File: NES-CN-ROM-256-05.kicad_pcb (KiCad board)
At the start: 2 copper layers, 100.3 x 54.9 mm, 14 parts, among them U2 74HC161, U3 ATtiny13A-PU, U4 CHR-ROM, U5 PRG-ROM

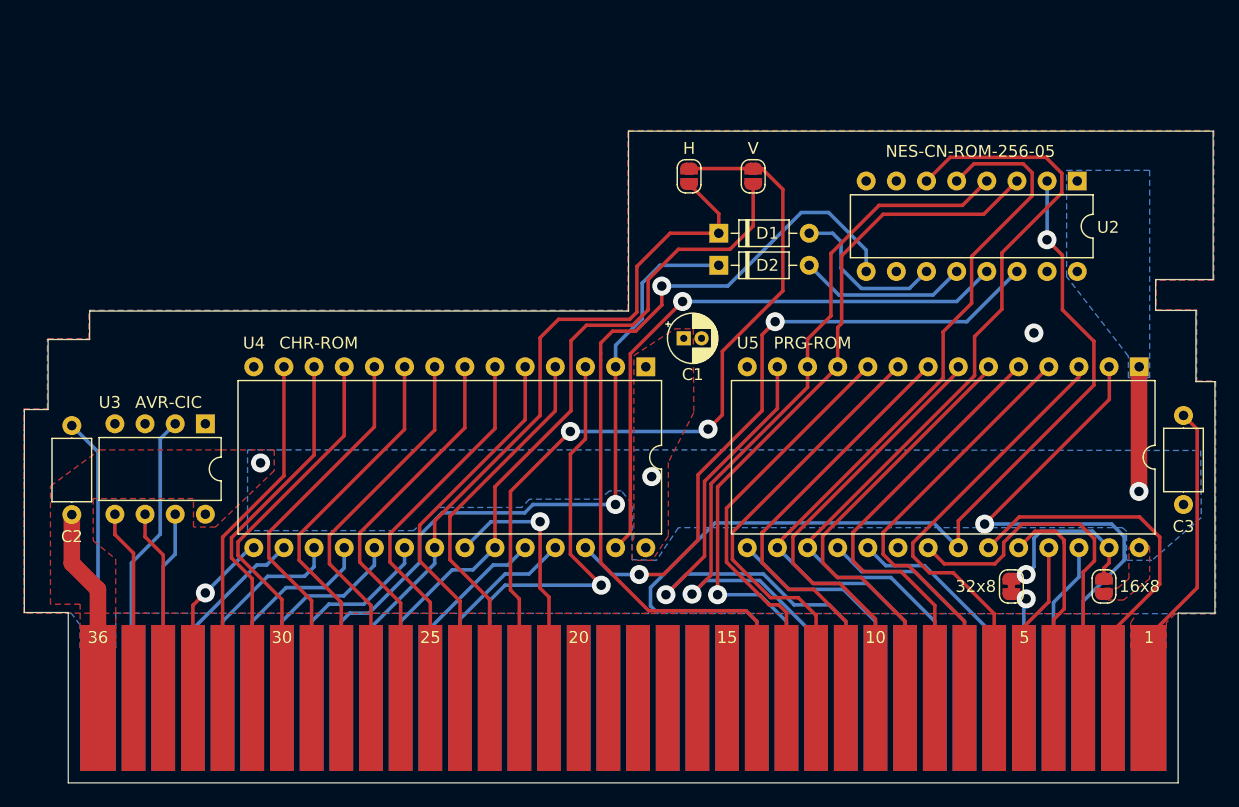
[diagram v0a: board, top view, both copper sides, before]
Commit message: [1] Change gerbers to protel file ext [2] Fix board dimensions [3] Add screenshot of jlcpcb order settings
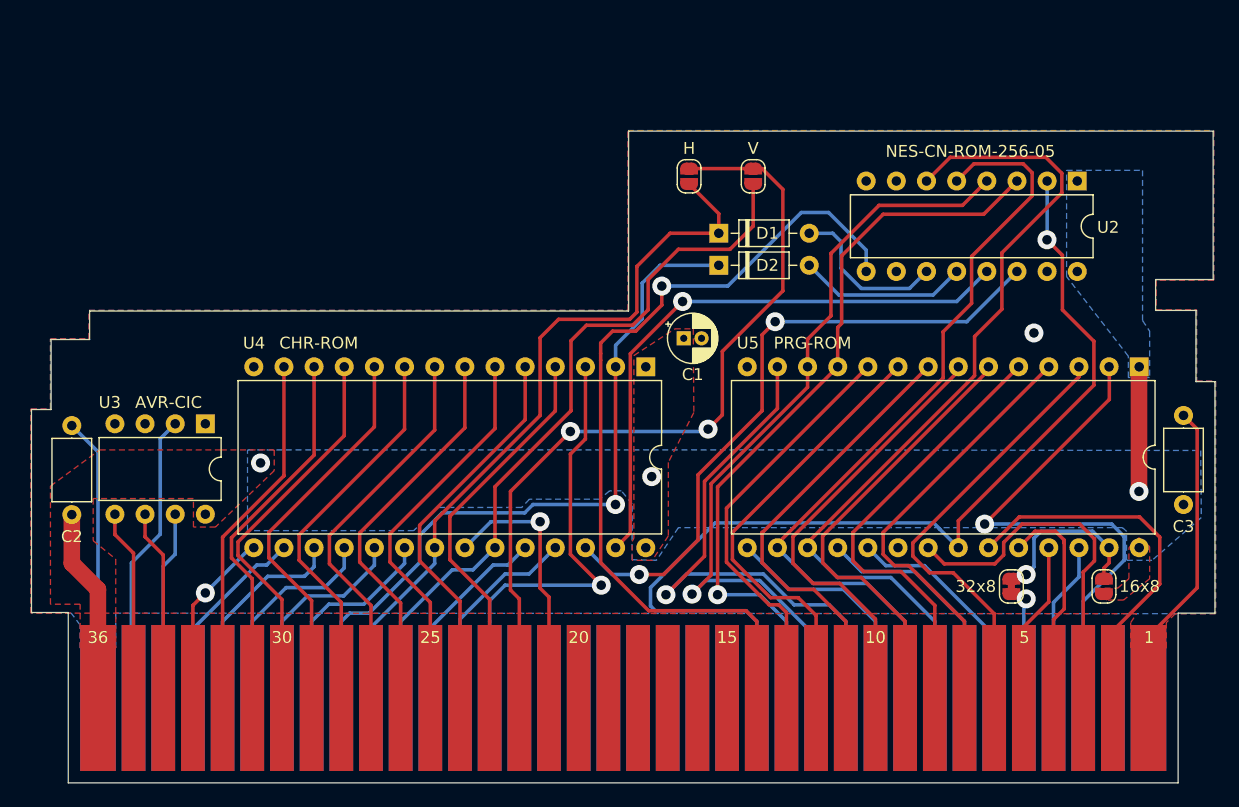
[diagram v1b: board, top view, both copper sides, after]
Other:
- board size 100.3 x 54.9 mm -> 99.7 x 54.9 mm
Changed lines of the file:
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@@
   (title_block
     (title "NES-CN-ROM-256-05 PCB")
-    (date 2022-04-25)
+    (date 2022-04-26)
     (rev v01)
     (comment 1 "License: https://creativecommons.org/licenses/by-sa/4.0/")
@@
     (visible_elements 7FFFFFFF)
     (pcbplotparams
-      (layerselection 0x010f0_ffffffff)
-      (usegerberextensions false)
-      (usegerberattributes true)
-      (usegerberadvancedattributes true)
+      (layerselection 0x010fc_ffffffff)
+      (usegerberextensions true)
+      (usegerberattributes false)
+      (usegerberadvancedattributes false)
       (creategerberjobfile false)
       (excludeedgelayer true)
@@
       (psa4output false)
       (plotreference true)
-      (plotvalue false)
+      (plotvalue true)
       (plotinvisibletext false)
       (padsonsilk false)
-      (subtractmaskfromsilk false)
+      (subtractmaskfromsilk true)
       (outputformat 1)
       (mirror false)
@@
       ))
   )
-  (dimension 3.7 (width 0.15) (layer Dwgs.User)
-    (gr_text "3.700 mm" (at 114.65 131.25) (layer Dwgs.User)
+  (dimension 3.1 (width 0.15) (layer Dwgs.User)
+    (gr_text "3.100 mm" (at 114.95 131.25) (layer Dwgs.User)
       (effects (font (size 1 1) (thickness 0.15)))
     )
     (feature1 (pts (xy 116.5 110.65) (xy 116.5 130.536421)))
-    (feature2 (pts (xy 112.8 110.65) (xy 112.8 130.536421)))
-    (crossbar (pts (xy 112.8 129.95) (xy 116.5 129.95)))
+    (feature2 (pts (xy 113.4 110.65) (xy 113.4 130.536421)))
+    (crossbar (pts (xy 113.4 129.95) (xy 116.5 129.95)))
     (arrow1a (pts (xy 116.5 129.95) (xy 115.373496 130.536421)))
     (arrow1b (pts (xy 116.5 129.95) (xy 115.373496 129.363579)))
-    (arrow2a (pts (xy 112.8 129.95) (xy 113.926504 130.536421)))
-    (arrow2b (pts (xy 112.8 129.95) (xy 113.926504 129.363579)))
+    (arrow2a (pts (xy 113.4 129.95) (xy 114.526504 130.536421)))
+    (arrow2b (pts (xy 113.4 129.95) (xy 114.526504 129.363579)))
   )
   (dimension 3.1 (width 0.15) (layer Dwgs.User)
@@
     (arrow2b (pts (xy 213.1 129.95) (xy 211.973496 130.536421)))
   )
-  (dimension 2 (width 0.15) (layer Dwgs.User)
-    (gr_text "2.000 mm" (at 113.8 82.7) (layer Dwgs.User)
-      (effects (font (size 1 1) (thickness 0.15)))
-    )
-    (feature1 (pts (xy 114.8 93.55) (xy 114.8 83.413579)))
-    (feature2 (pts (xy 112.8 93.55) (xy 112.8 83.413579)))
-    (crossbar (pts (xy 112.8 84) (xy 114.8 84)))
-    (arrow1a (pts (xy 114.8 84) (xy 113.673496 84.586421)))
-    (arrow1b (pts (xy 114.8 84) (xy 113.673496 83.413579)))
-    (arrow2a (pts (xy 112.8 84) (xy 113.926504 84.586421)))
-    (arrow2b (pts (xy 112.8 84) (xy 113.926504 83.413579)))
+  (dimension 1.65 (width 0.15) (layer Dwgs.User)
+    (gr_text "1.650 mm" (at 114.225 82.7) (layer Dwgs.User)
+      (effects (font (size 1 1) (thickness 0.15)))
+    )
+    (feature1 (pts (xy 115.05 93.55) (xy 115.05 83.413579)))
+    (feature2 (pts (xy 113.4 93.55) (xy 113.4 83.413579)))
+    (crossbar (pts (xy 113.4 84) (xy 115.05 84)))
+    (arrow1a (pts (xy 115.05 84) (xy 113.923496 84.586421)))
+    (arrow1b (pts (xy 115.05 84) (xy 113.923496 83.413579)))
+    (arrow2a (pts (xy 113.4 84) (xy 114.526504 84.586421)))
+    (arrow2b (pts (xy 113.4 84) (xy 114.526504 83.413579)))
   )
   (dimension 45.4 (width 0.15) (layer Dwgs.User)
@@
     (arrow2b (pts (xy 118.3 66.5) (xy 119.426504 65.913579)))
   )
-  (dimension 3.5 (width 0.15) (layer Dwgs.User)
-    (gr_text "3.500 mm" (at 116.55 78.7) (layer Dwgs.User)
+  (dimension 3.25 (width 0.15) (layer Dwgs.User)
+    (gr_text "3.250 mm" (at 116.675 78.7) (layer Dwgs.User)
       (effects (font (size 1 1) (thickness 0.15)))
     )
     (feature1 (pts (xy 118.3 87.65) (xy 118.3 79.413579)))
-    (feature2 (pts (xy 114.8 87.65) (xy 114.8 79.413579)))
-    (crossbar (pts (xy 114.8 80) (xy 118.3 80)))
+    (feature2 (pts (xy 115.05 87.65) (xy 115.05 79.413579)))
+    (crossbar (pts (xy 115.05 80) (xy 118.3 80)))
     (arrow1a (pts (xy 118.3 80) (xy 117.173496 80.586421)))
     (arrow1b (pts (xy 118.3 80) (xy 117.173496 79.413579)))
-    (arrow2a (pts (xy 114.8 80) (xy 115.926504 80.586421)))
-    (arrow2b (pts (xy 114.8 80) (xy 115.926504 79.413579)))
+    (arrow2a (pts (xy 115.05 80) (xy 116.176504 80.586421)))
+    (arrow2b (pts (xy 115.05 80) (xy 116.176504 79.413579)))
   )
   (dimension 5.9 (width 0.15) (layer Dwgs.User)
@@
   )
   (gr_line (start 116.5 110.65) (end 116.5 110.7) (layer Edge.Cuts) (width 0.05))
-  (gr_line (start 112.8 110.65) (end 116.5 110.65) (layer Edge.Cuts) (width 0.05))
-  (gr_line (start 112.8 93.55) (end 112.8 110.65) (layer Edge.Cuts) (width 0.05))
-  (gr_line (start 114.8 93.55) (end 112.8 93.55) (layer Edge.Cuts) (width 0.05))
-  (gr_line (start 114.8 87.65) (end 114.8 93.55) (layer Edge.Cuts) (width 0.05))
-  (gr_line (start 118.3 87.65) (end 114.8 87.65) (layer Edge.Cuts) (width 0.05))
+  (gr_line (start 113.4 110.65) (end 116.5 110.65) (layer Edge.Cuts) (width 0.05))
+  (gr_line (start 113.4 93.55) (end 113.4 110.65) (layer Edge.Cuts) (width 0.05))
+  (gr_line (start 115.05 93.55) (end 113.4 93.55) (layer Edge.Cuts) (width 0.05))
+  (gr_line (start 115.05 87.65) (end 115.05 93.55) (layer Edge.Cuts) (width 0.05))
+  (gr_line (start 118.3 87.65) (end 115.05 87.65) (layer Edge.Cuts) (width 0.05))
   (gr_line (start 118.3 85.25) (end 118.3 87.65) (layer Edge.Cuts) (width 0.05))
   (gr_line (start 163.7 85.25) (end 118.3 85.25) (layer Edge.Cuts) (width 0.05))
@@
     (polygon
       (pts
-        (xy 207.6 90.85) (xy 205.8 90.85) (xy 205.8 89.05) (xy 200.6 82.35) (xy 200.6 73.4)
-        (xy 207.6 73.4)
+        (xy 207 86.05) (xy 207.6 86.95) (xy 207.6 90.85) (xy 205.8 90.85) (xy 205.8 89.05)
+        (xy 200.6 82.35) (xy 200.6 73.4) (xy 207 73.4)
       )
     )
@@
         (xy 213 82.65) (xy 208.15 82.65) (xy 208.15 85.15) (xy 211.55 85.15) (xy 211.55 91.15)
         (xy 213.15 91.15) (xy 213.15 110.75) (xy 209.75 110.75) (xy 209 111.5) (xy 209 113.65)
-        (xy 206 113.65) (xy 206 111.5) (xy 206.5 110.75) (xy 112.75 110.7) (xy 112.75 93.5)
-        (xy 114.75 93.5) (xy 114.75 87.6) (xy 118.25 87.6) (xy 118.25 85.2) (xy 163.65 85.2)
+        (xy 206 113.65) (xy 206 111.5) (xy 206.5 110.75) (xy 113.35 110.7) (xy 113.35 93.5)
+        (xy 115 93.5) (xy 115 87.6) (xy 118.25 87.6) (xy 118.25 85.2) (xy 163.65 85.2)
         (xy 163.65 70.05) (xy 213 70.05)
       )
@@
         (xy 213 82.65) (xy 208.15 82.65) (xy 208.15 85.15) (xy 211.55 85.15) (xy 211.55 91.15)
         (xy 213.15 91.15) (xy 213.15 110.75) (xy 120.5 110.70401) (xy 120.5 113.65) (xy 117.5 113.65)
-        (xy 117.5 111.7) (xy 116.75 110.7) (xy 112.75 110.7) (xy 112.75 93.5) (xy 114.75 93.5)
-        (xy 114.75 87.6) (xy 118.25 87.6) (xy 118.25 85.2) (xy 163.65 85.2) (xy 163.65 70.05)
+        (xy 117.5 111.7) (xy 116.75 110.7) (xy 113.35 110.7) (xy 113.35 93.5) (xy 115 93.5)
+        (xy 115 87.6) (xy 118.25 87.6) (xy 118.25 85.2) (xy 163.65 85.2) (xy 163.65 70.05)
         (xy 213 70.05)
       )

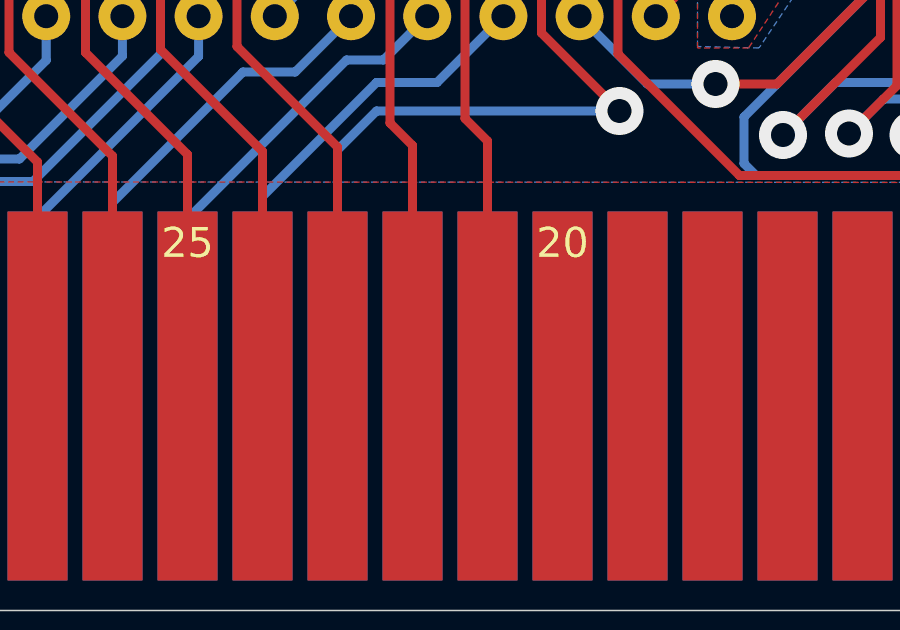
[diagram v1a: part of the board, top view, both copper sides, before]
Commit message: [1] Connect cartridge pins 57-58 for NES internal VRAM enable line. [2] Regenerate gerbers.
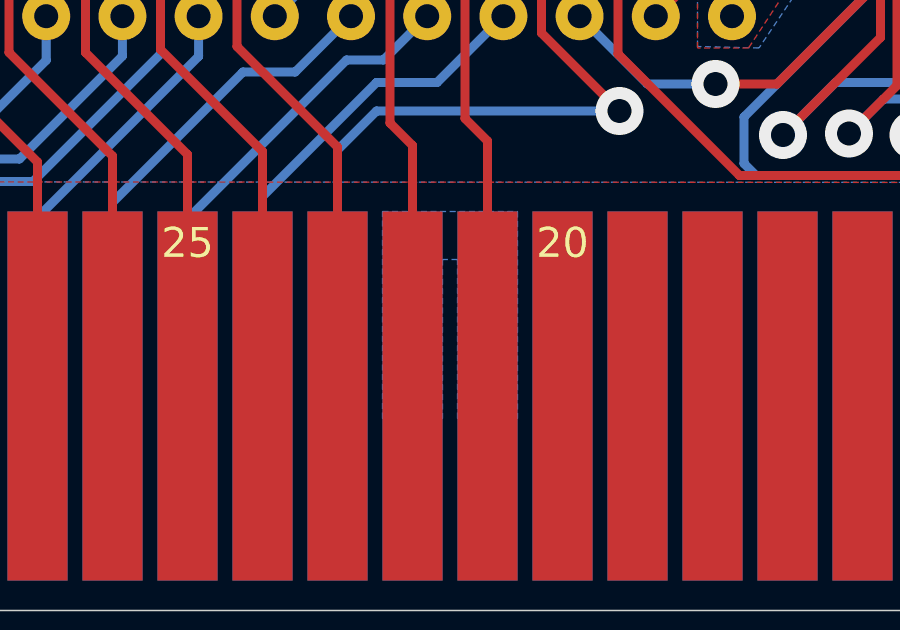
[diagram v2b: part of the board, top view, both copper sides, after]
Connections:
- EDGE1 pad 57: (no net) -> Net-(EDGE1-Pad57)
- EDGE1 pad 58: (no net) -> Net-(EDGE1-Pad57)
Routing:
- added copper zone on B.Cu, net Net-(EDGE1-Pad57)
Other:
- net class VRAM_Enable added: clearance 0.2, trace_width 2, via_dia 1.6, via_drill 0.8
- board text added: "v01.1"
- board text removed: "v01"

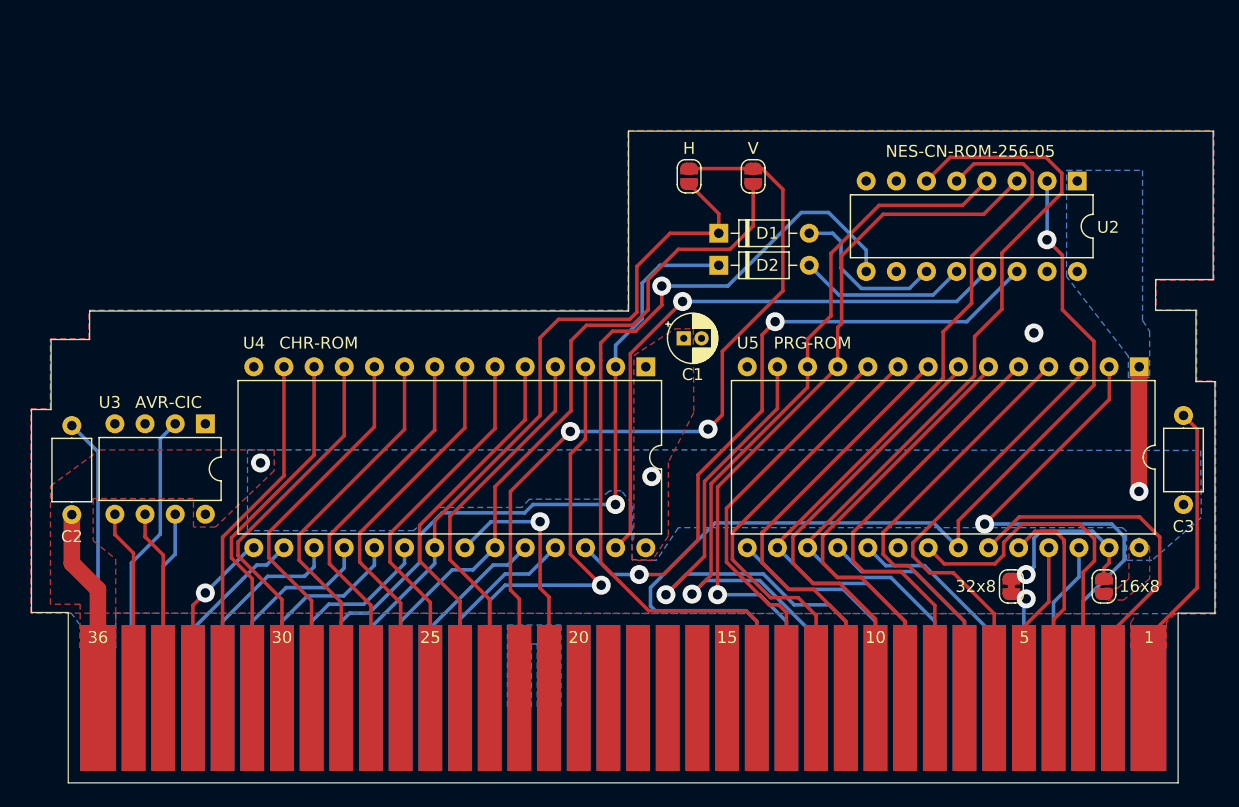
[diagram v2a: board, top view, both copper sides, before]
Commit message: New board layout to support 32 dip flash chips
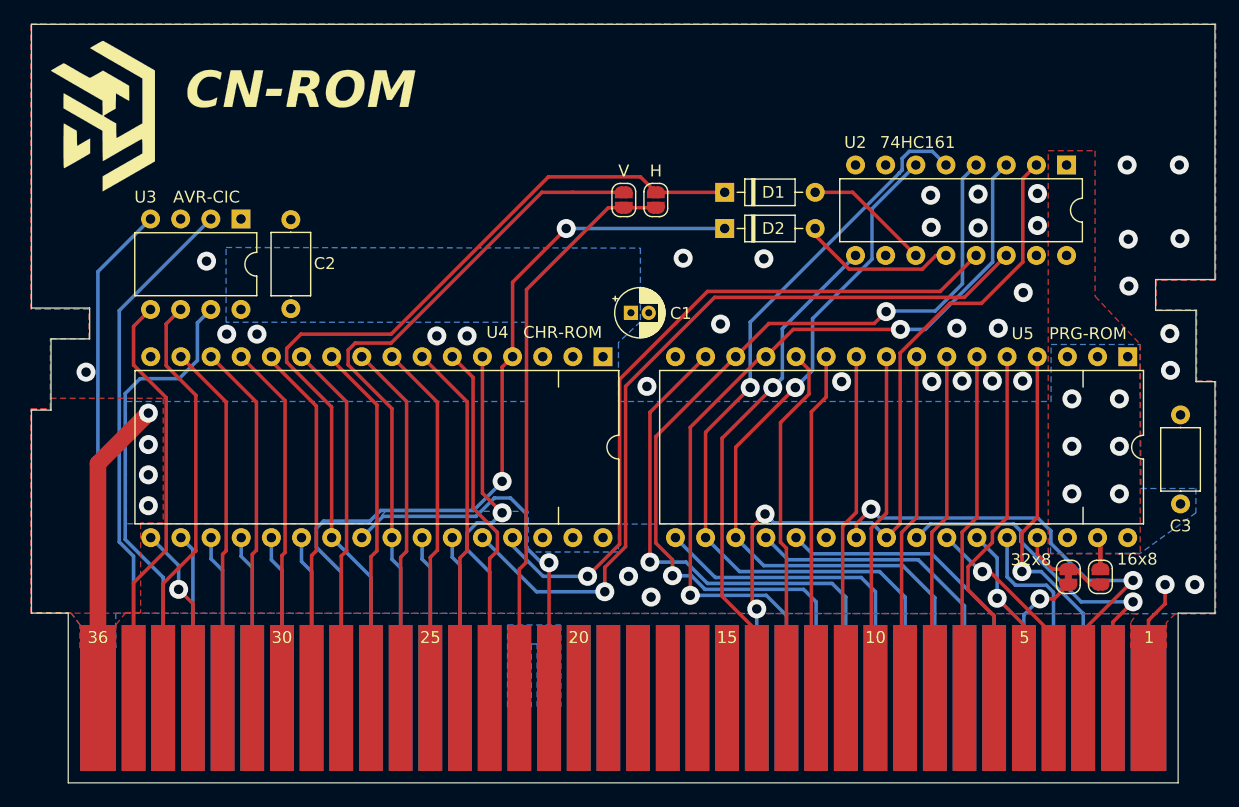
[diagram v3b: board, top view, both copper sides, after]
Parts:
- added G1: LOGO, logo:flash_logo, F.Cu at (119.4, 69.5)
- added G2: LOGO, logo:flash_negative_logo, F.Cu at (119.4, 69.5)
- added G3: LOGO, logo:cnrom_text, F.Cu at (136.0, 66.5)
- U4, U5: footprint Package_DIP:DIP-28_W15.24mm -> Package_DIP:DIP-32_W15.24mm
- moved C2 25.3 mm to (135.2, 85.0)
- moved U3 17.5 mm to (131.1, 77.5)
- moved JP4 11.1 mm to (163.3, 75.9), turned to 270 degrees
- moved C1 4.94 mm to (163.9, 85.4)
- moved JP1 4.87 mm to (200.8, 107.7)
- moved U4 3.70 mm to (161.6, 89.1)
- moved D1 3.49 mm to (171.8, 75.2)
- moved JP3 3.44 mm to (166.0, 75.9), turned to 270 degrees
- moved D2 3.14 mm to (171.8, 78.3)
- moved U2 1.62 mm to (200.6, 73.0)
- moved U5 1.29 mm to (205.8, 89.1)
- moved JP2 0.85 mm to (203.4, 107.7), turned to 270 degrees
- moved C3 0.25 mm to (210.2, 101.5)
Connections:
- U4 pad 10: PPU_A0 -> PPU_A2
- U4 pad 11: PPU_AD0 -> PPU_A1
- U4 pad 12: PPU_AD1 -> PPU_A0
- U4 pad 13: PPU_AD2 -> PPU_AD0
- U4 pad 14: GND -> PPU_AD1
- U4 pad 15: PPU_AD3 -> PPU_AD2
- U4 pad 16: PPU_AD4 -> GND
- U4 pad 17: PPU_AD5 -> PPU_AD3
- U4 pad 18: PPU_AD6 -> PPU_AD4
- U4 pad 19: PPU_AD7 -> PPU_AD5
- U4 pad 2: PPU_A12 -> +5V
- U4 pad 20: PPU_A13 -> PPU_AD6
- U4 pad 21: PPU_A10 -> PPU_AD7
- U4 pad 22: PPU_RD -> PPU_A13
- U4 pad 23: PPU_A11 -> PPU_A10
- U4 pad 24: PPU_A9 -> PPU_RD
- U4 pad 25: PPU_A8 -> PPU_A11
- U4 pad 26: /CHR_A13 -> PPU_A9
- U4 pad 27: /CHR_A14 -> PPU_A8
- U4 pad 28: +5V -> /CHR_A13
- U4 pad 3: PPU_A7 -> +5V
- U4 pad 4: PPU_A6 -> PPU_A12
- U4 pad 5: PPU_A5 -> PPU_A7
- U4 pad 6: PPU_A4 -> PPU_A6
- U4 pad 7: PPU_A3 -> PPU_A5
- U4 pad 8: PPU_A2 -> PPU_A4
- U4 pad 9: PPU_A1 -> PPU_A3
- U5 pad 10: CPU_A0 -> CPU_A2
- U5 pad 11: CPU_D0 -> CPU_A1
- U5 pad 12: CPU_D1 -> CPU_A0
- U5 pad 13: CPU_D2 -> CPU_D0
- U5 pad 14: GND -> CPU_D1
- U5 pad 15: CPU_D3 -> CPU_D2
- U5 pad 16: CPU_D4 -> GND
- U5 pad 17: CPU_D5 -> CPU_D3
- U5 pad 18: CPU_D6 -> CPU_D4
- U5 pad 19: CPU_D7 -> CPU_D5
- U5 pad 2: CPU_A12 -> +5V
- U5 pad 20: GND -> CPU_D6
- U5 pad 21: CPU_A10 -> CPU_D7
- U5 pad 22: ROMSEL -> GND
- U5 pad 23: CPU_A11 -> CPU_A10
- U5 pad 24: CPU_A9 -> ROMSEL
- U5 pad 25: CPU_A8 -> CPU_A11
- U5 pad 26: CPU_A13 -> CPU_A9
- U5 pad 27: /PRG_A14 -> CPU_A8
- U5 pad 28: +5V -> CPU_A13
- U5 pad 3: CPU_A7 -> +5V
- U5 pad 4: CPU_A6 -> CPU_A12
- U5 pad 5: CPU_A5 -> CPU_A7
- U5 pad 6: CPU_A4 -> CPU_A6
- U5 pad 7: CPU_A3 -> CPU_A5
- U5 pad 8: CPU_A2 -> CPU_A4
- U5 pad 9: CPU_A1 -> CPU_A3
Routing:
- net CPU_RW: track 71.1 -> 43.1 mm
- net CIC_RST: track 15.9 -> 39.0 mm
- net CIRAM_A10: track 68.0 -> 48.4 mm, vias 2 -> 0
- net CIC_IN: track 16.1 -> 35.6 mm
- net CIC_CLK: track 24.7 -> 44.0 mm
- net CIC_OUT: track 16.1 -> 35.4 mm
- net ROMSEL: track 83.8 -> 65.3 mm, vias 1 -> 2
- net PPU_A10: track 62.4 -> 75.8 mm
- net /CHR_A13: track 54.8 -> 66.9 mm, vias 2 -> 1
- net /CHR_A14: track 49.8 -> 60.1 mm
- net PPU_RD: track 22.4 -> 32.5 mm
- net CPU_A5: track 38.4 -> 29.4 mm
- net CPU_A10: track 30.9 -> 39.7 mm, vias 0 -> 2
- net CPU_A1: track 38.0 -> 29.4 mm
- net CPU_A2: track 37.9 -> 29.3 mm
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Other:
- board size 99.7 x 54.9 mm -> 99.7 x 63.9 mm
- net class VRAM_Enable: trace_width 2 -> 0.4
- board text added: "2022-07-30"
- board text added: "v02"
- board text removed: "v01.1"
